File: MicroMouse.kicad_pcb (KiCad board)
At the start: 2 copper layers, 100 x 80 mm, 81 parts, among them CN1 mouseBattery, Q1 IRLML6402, Q2 IRLML6344, SW1 SPST, SW2 SPST, SW3 SPST, U1 STM32F405RGTx, U2 TB6612, U3 CN_MOTOR, U4 CN_MOTOR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

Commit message: ハイパー配線タイム
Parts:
- moved D2 4.03 mm to (13.0, 14.0)
- moved R3 3.89 mm to (15.0, 16.0)
- moved R4 3.88 mm to (15.0, 64.0)
- moved D3 3.86 mm to (13.0, 66.0)
- moved R6 1.73 mm to (30.0, 74.0)
- moved D5 1.66 mm to (30.0, 76.0)
- moved D1 0.83 mm to (3.00, 40.0)
- moved R5 0.75 mm to (30.0, 6.00)
- moved R2 0.62 mm to (12.0, 40.0)
- moved D4 0.35 mm to (30.0, 4.00)

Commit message: 信号線を引いていく
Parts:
- moved R27 1.00 mm to (19.0, 33.0)
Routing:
- net +3V3: track 0.00 -> 339.5 mm, vias 0 -> 8
- net +5V: track 0.00 -> 281.1 mm, vias 0 -> 5
- net VCC: track 0.00 -> 71.1 mm, vias 0 -> 2
- net SEN_LF: track 0.00 -> 16.5 mm
- net Net-(CN1-Pad1): track 0.00 -> 14.5 mm, vias 0 -> 1
- net Net-(Q1-Pad1): track 0.00 -> 10.8 mm
- net Net-(Q2-Pad1): track 0.00 -> 7.56 mm
- net Net-(D1-Pad2): track 0.00 -> 6.80 mm
- net Net-(OPAMP2-Pad5): track 0.00 -> 5.57 mm
- net Net-(OPAMP1-Pad5): track 0.00 -> 5.57 mm
- net NRST: track 0.00 -> 4.65 mm
- net Mode_SW: track 0.00 -> 4.65 mm
- net Net-(Q2-Pad3): track 0.00 -> 4.21 mm
- net BOOT0: track 0.00 -> 4.15 mm
- net Net-(D11-Pad1): track 0.00 -> 3.88 mm
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- added copper zone on B.Cu, net GND

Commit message: ビア撃ちマン
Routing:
- net NRST: track 4.65 -> 124.1 mm, vias 0 -> 4
- net USART1_TX: track 0.00 -> 95.7 mm, vias 0 -> 3
- net USART1_RX: track 0.00 -> 95.3 mm, vias 0 -> 3
- net R_ENC_B: track 0.00 -> 82.6 mm, vias 0 -> 3
- net R_ENC_A: track 0.00 -> 81.6 mm, vias 0 -> 3
- net SWCLK: track 0.00 -> 80.0 mm, vias 0 -> 3
- net SWDIO: track 0.00 -> 74.6 mm, vias 0 -> 3
- net L_ENC_B: track 0.00 -> 72.4 mm, vias 0 -> 3
- net L_ENC_A: track 0.00 -> 72.1 mm, vias 0 -> 3
- net SPK: track 0.00 -> 69.3 mm, vias 0 -> 2
- net M_STBY: track 0.00 -> 68.4 mm, vias 0 -> 2
- net M_IN1_R: track 0.00 -> 67.4 mm, vias 0 -> 2
- net M_IN2_R: track 0.00 -> 66.2 mm, vias 0 -> 2
- net M_IN2_L: track 0.00 -> 65.7 mm
- net M_IN1_L: track 0.00 -> 65.3 mm
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
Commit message: GND強化していこうな
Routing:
- net GND: track 41.5 -> 34.3 mm, vias 18 -> 46
- net M_IN1_R: track 67.4 -> 68.8 mm
- net M_IN2_R: track 66.2 -> 67.0 mm

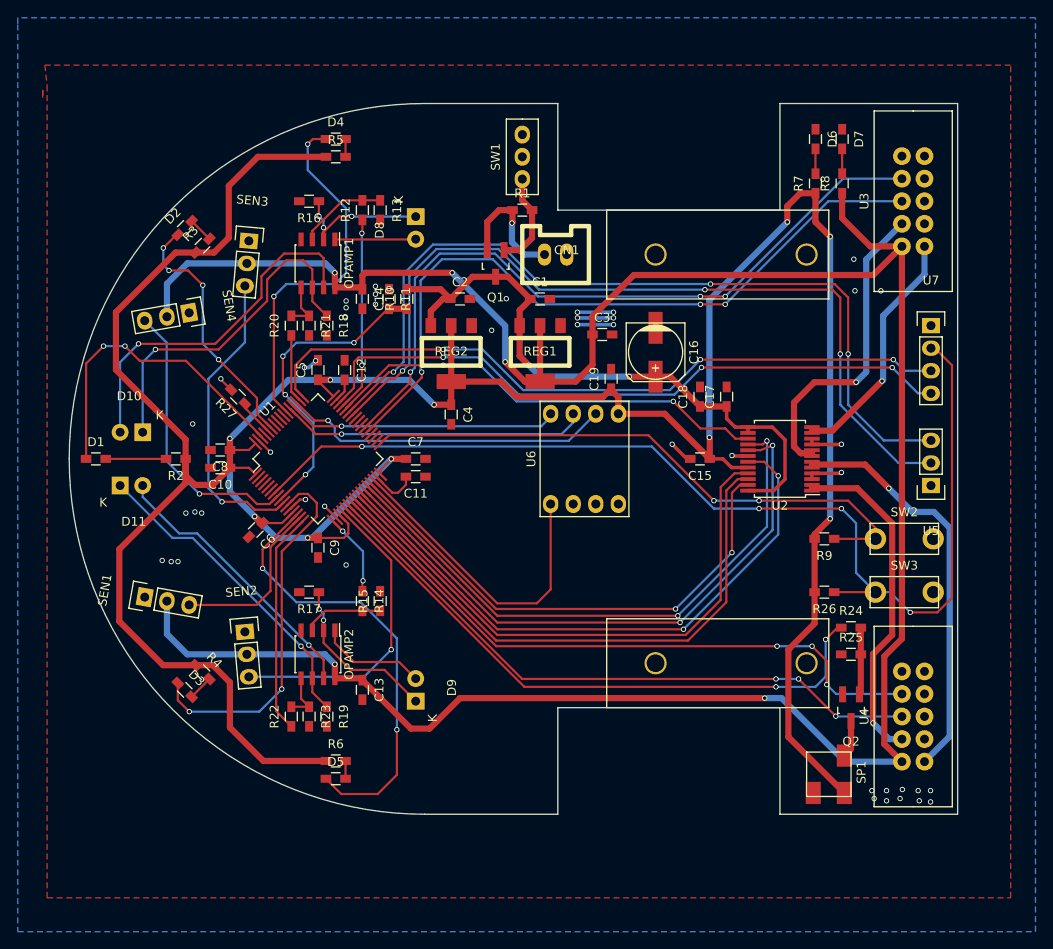
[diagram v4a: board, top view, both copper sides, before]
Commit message: GNDを強化
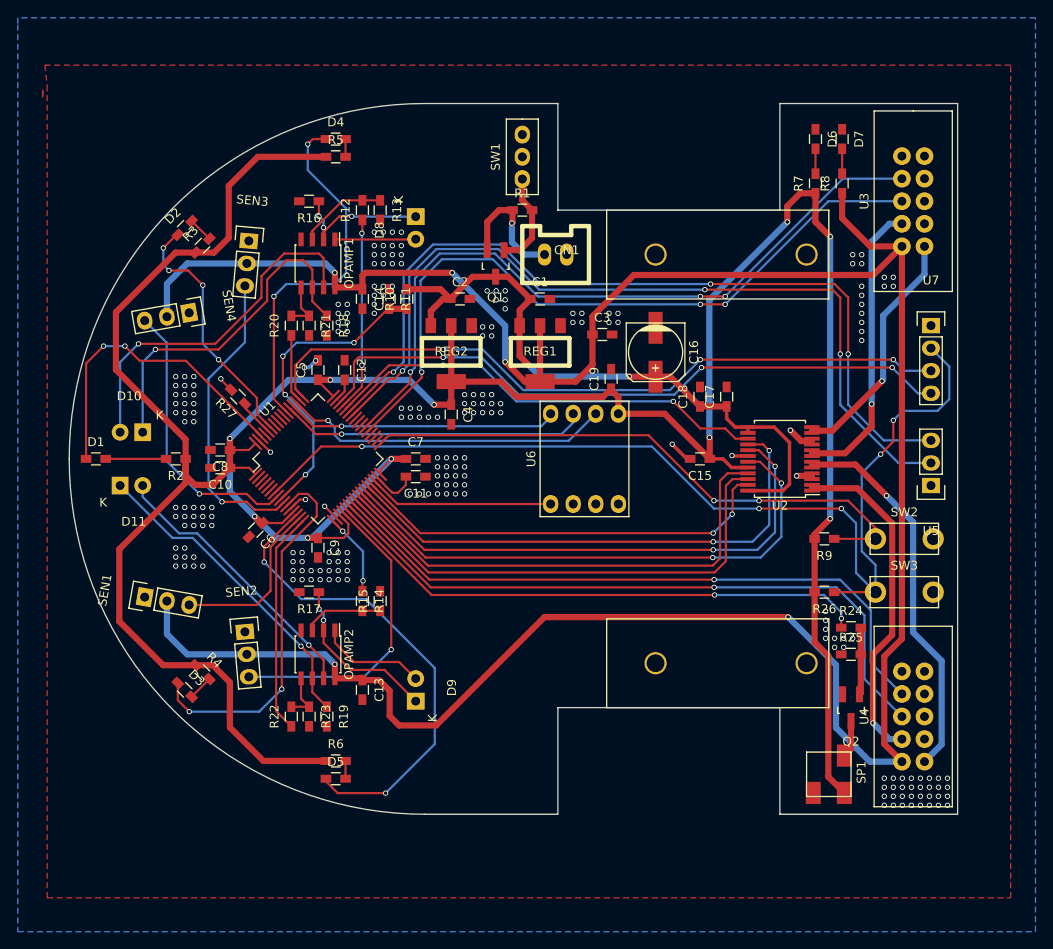
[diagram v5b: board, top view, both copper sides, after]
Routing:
- net CS: track 35.9 -> 21.0 mm
- net GND: track 34.3 -> 20.0 mm, vias 46 -> 225
- net +5V: track 281.1 -> 294.2 mm
- net M_PWM_L: track 58.0 -> 48.6 mm
- net M_IN1_L: track 65.3 -> 56.5 mm
- net M_IN2_L: track 65.7 -> 56.9 mm
- net M_IN1_R: track 68.8 -> 61.0 mm
- net M_IN2_R: track 67.0 -> 59.6 mm
- net SPK: track 69.3 -> 62.3 mm
- net M_STBY: track 68.4 -> 62.1 mm
- net NRST: track 124.1 -> 119.9 mm, vias 4 -> 5
- net L_ENC_A: track 72.1 -> 76.3 mm, vias 3 -> 1
- net DBG_LED_5: track 50.9 -> 54.9 mm
- net Net-(U2-Pad5): track 46.6 -> 43.8 mm
- net +3V3: track 361.8 -> 359.4 mm
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
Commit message: あとはビアの調整
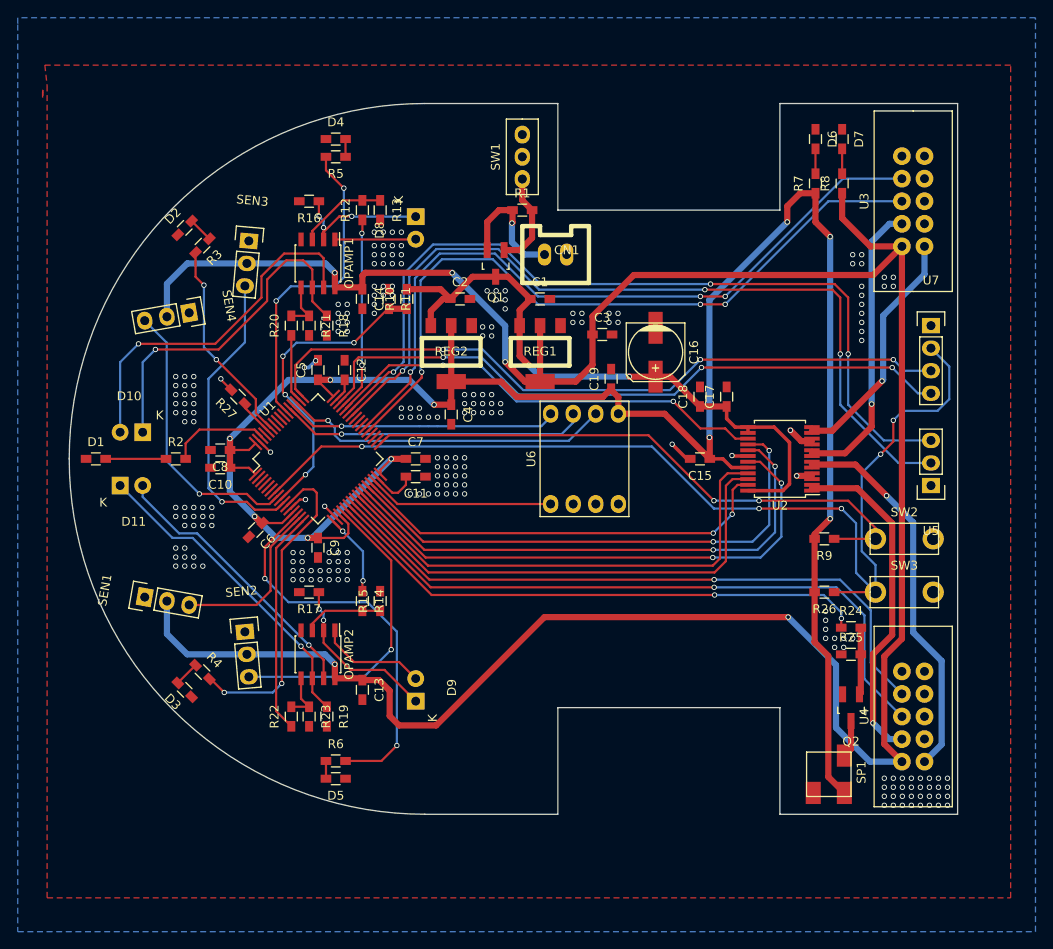
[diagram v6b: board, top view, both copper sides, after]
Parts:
- removed REF** (x2): motormount, myfootprint:motormount
- turned D3 to 135 degrees
- turned D5 to 180 degrees
- turned R2 to 0 degrees
- turned R3 to 225 degrees
- turned R5 to 180 degrees
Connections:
- C6 pad 2: GND -> (no net)
- D1 pad 1: DBG_LED_1 -> GND
- D2 pad 1: DBG_LED_2 -> GND
- D3 pad 1: DBG_LED_3 -> GND
- D4 pad 1: DBG_LED_4 -> GND
- D5 pad 1: DBG_LED_5 -> GND
- R2 pad 1: +3V3 -> Net-(D1-Pad2)
- R2 pad 2: Net-(D1-Pad2) -> DBG_LED_1
- R3 pad 1: +3V3 -> Net-(D2-Pad2)
- R3 pad 2: Net-(D2-Pad2) -> DBG_LED_2
- R4 pad 1: +3V3 -> Net-(D3-Pad2)
- R4 pad 2: Net-(D3-Pad2) -> DBG_LED_3
- R5 pad 1: +3V3 -> Net-(D4-Pad2)
- R5 pad 2: Net-(D4-Pad2) -> DBG_LED_4
- R6 pad 1: +3V3 -> Net-(D5-Pad2)
- R6 pad 2: Net-(D5-Pad2) -> DBG_LED_5
- U1 pad 2: Net-(U1-Pad2) -> (no net)
- U1 pad 3: Net-(U1-Pad3) -> (no net)
- U1 pad 34: Net-(U1-Pad34) -> (no net)
- U1 pad 35: Net-(U1-Pad35) -> (no net)
- U1 pad 36: Net-(U1-Pad36) -> (no net)
- U1 pad 39: Net-(U1-Pad39) -> (no net)
- U1 pad 4: Net-(U1-Pad4) -> (no net)
- U1 pad 40: Net-(U1-Pad40) -> (no net)
- U1 pad 41: Net-(U1-Pad41) -> (no net)
- U1 pad 5: Net-(U1-Pad5) -> (no net)
- U1 pad 55: Net-(U1-Pad55) -> (no net)
- U1 pad 56: Net-(U1-Pad56) -> (no net)
- U1 pad 57: Net-(U1-Pad57) -> (no net)
- U1 pad 58: Net-(U1-Pad58) -> (no net)
- U1 pad 6: Net-(U1-Pad6) -> (no net)
- U1 pad 61: Net-(U1-Pad61) -> (no net)
- U3 pad 10: Net-(U3-Pad10) -> (no net)
- U3 pad 5: Net-(U3-Pad5) -> (no net)
- U3 pad 7: Net-(U3-Pad7) -> (no net)
- U3 pad 9: Net-(U3-Pad9) -> (no net)
- U4 pad 10: Net-(U4-Pad10) -> (no net)
- U4 pad 5: Net-(U4-Pad5) -> (no net)
- U4 pad 7: Net-(U4-Pad7) -> (no net)
- U4 pad 9: Net-(U4-Pad9) -> (no net)
- U6 pad 6: Net-(U6-Pad6) -> (no net)
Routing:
- net +3V3: track 359.4 -> 243.1 mm
- net DBG_LED_1: track 35.6 -> 11.4 mm, vias 2 -> 0
- net DBG_LED_5: track 54.9 -> 45.3 mm
- net DBG_LED_3: track 42.2 -> 36.6 mm
- net DBG_LED_2: track 28.8 -> 23.3 mm, vias 4 -> 2
- net DBG_LED_4: track 41.4 -> 36.1 mm

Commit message: モータマウント取れてた
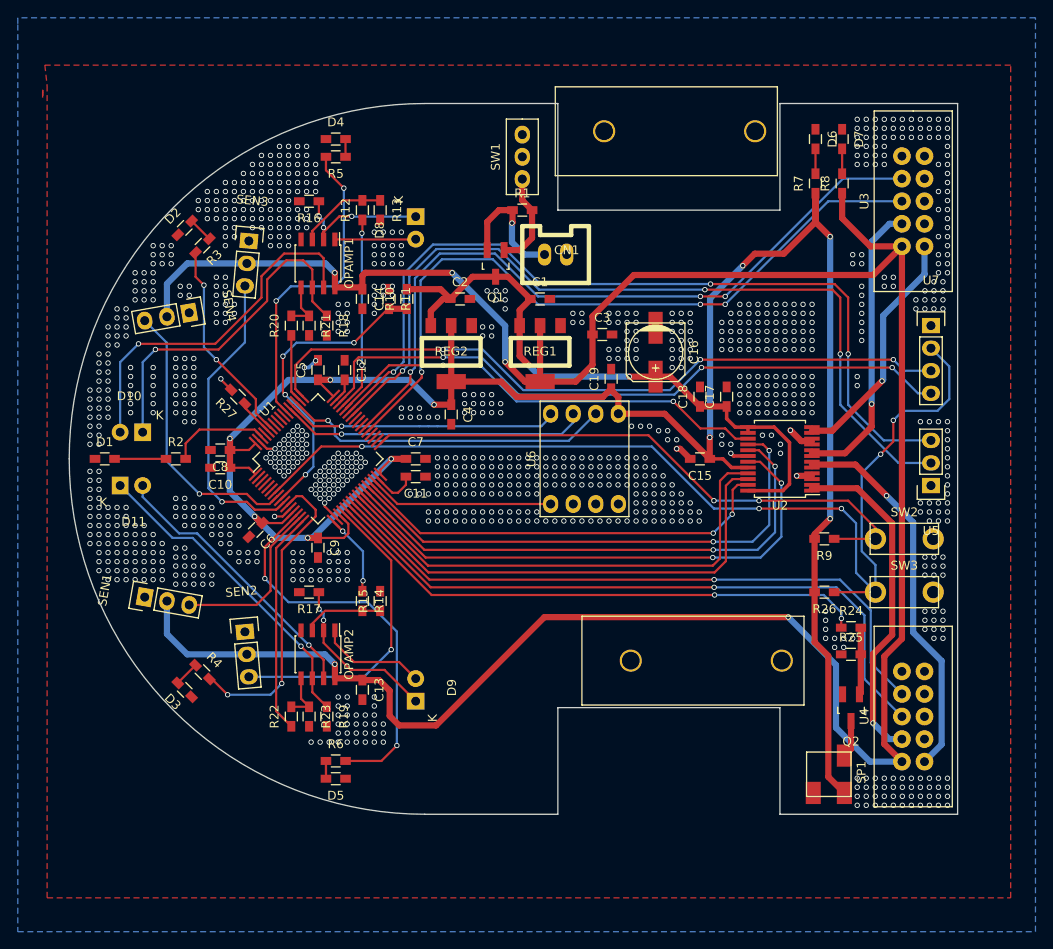
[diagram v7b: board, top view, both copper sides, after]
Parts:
- added REF**: motormount, myfootprint:motormount, F.Cu at (54.7, -1.88)
- added REF**: motormount, myfootprint:motormount, F.Cu at (57.7, 57.7)
- moved D1 1.00 mm to (4.00, 40.0)
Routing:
- net DBG_LED_3: track 36.6 -> 34.9 mm
- net Net-(D1-Pad2): track 6.80 -> 5.80 mm
- net +3V3: track 243.1 -> 244.0 mm
- net GND: track 20.0 -> 20.6 mm, vias 225 -> 1094

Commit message: ビア打ちまくったマン 最終確認
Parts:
- moved REF** 15.0 mm to (60.5, 12.0)
- moved R13 7.00 mm to (28.0, 12.0), turned to 0 degrees
- moved R15 7.00 mm to (28.0, 56.0), turned to 0 degrees
- moved R16 6.00 mm to (33.0, 11.0)
- moved R17 6.00 mm to (33.0, 55.0)
- moved R12 5.39 mm to (28.0, 10.0), turned to 180 degrees
- moved R14 5.39 mm to (28.0, 54.0), turned to 180 degrees
- moved REF** 2.81 mm to (60.5, 58.0)
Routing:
- net LED_RS: track 21.8 -> 35.8 mm
- net Net-(OPAMP1-Pad3): track 10.0 -> 5.49 mm
- net Net-(D9-Pad1): track 19.0 -> 23.3 mm, vias 2 -> 0
- net Net-(D10-Pad2): track 40.8 -> 36.8 mm, vias 1 -> 0
- net Net-(OPAMP2-Pad3): track 8.99 -> 5.49 mm
- net Net-(D10-Pad1): track 39.5 -> 36.3 mm, vias 1 -> 0
- net Net-(D8-Pad1): track 16.5 -> 14.3 mm, vias 3 -> 0
- net +3V3: track 244.0 -> 245.3 mm
- net LED_LS: track 9.28 -> 8.41 mm
- net LED_LF: track 25.0 -> 25.8 mm, vias 0 -> 2
- net +5V: track 294.2 -> 293.4 mm, vias 5 -> 3
- net DBG_LED_3: track 34.9 -> 34.2 mm
- net GND: vias 1094 -> 2062
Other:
- rule trace_min: 0.1524 -> 0.203
- rule via_min_size: 0.5 -> 0.6
